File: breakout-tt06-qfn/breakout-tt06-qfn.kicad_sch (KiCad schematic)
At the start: 42 parts, among them J1 Conn_01x04, U1 Openframe_QFN_TT06_REV2, U2 24LC02

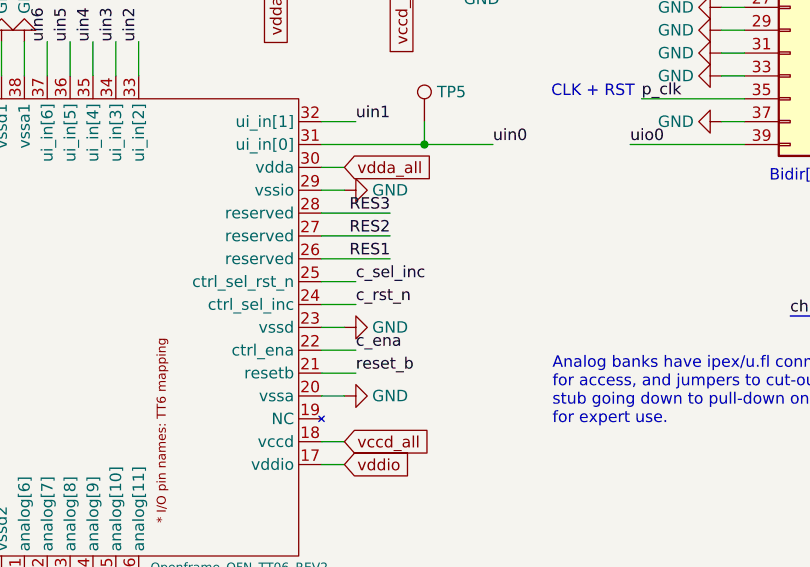
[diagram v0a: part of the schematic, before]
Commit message: CTRL MUX nReset and Increment lines crossed at chip: fixed
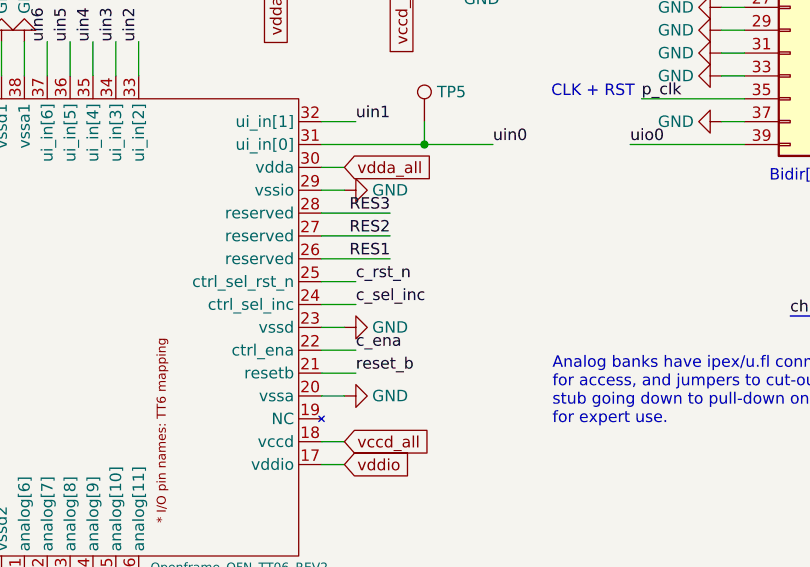
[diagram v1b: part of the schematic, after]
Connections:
- net c_rst_n: now also U1.25 (ctrl_sel_rst_n); no longer U1.24 (ctrl_sel_inc)
- net c_sel_inc: now also U1.24 (ctrl_sel_inc); no longer U1.25 (ctrl_sel_rst_n)
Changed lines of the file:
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@@
 	(title_block
 		(title "TT06 Openframe breakout")
-		(date "2024-08-10")
-		(rev "1.0")
+		(date "2024-11-04")
+		(rev "1.1")
 		(company "Psychogenic Technologies")
 		(comment 1 "(C) 2024 Pat Deegan")
@@
 		)
 	)
-	(label "c_sel_inc"
+	(label "c_rst_n"
 		(at 130.81 91.44 0)
 		(fields_autoplaced yes)
@@
 		)
 	)
-	(label "c_rst_n"
+	(label "c_sel_inc"
 		(at 130.81 93.98 0)
 		(fields_autoplaced yes)

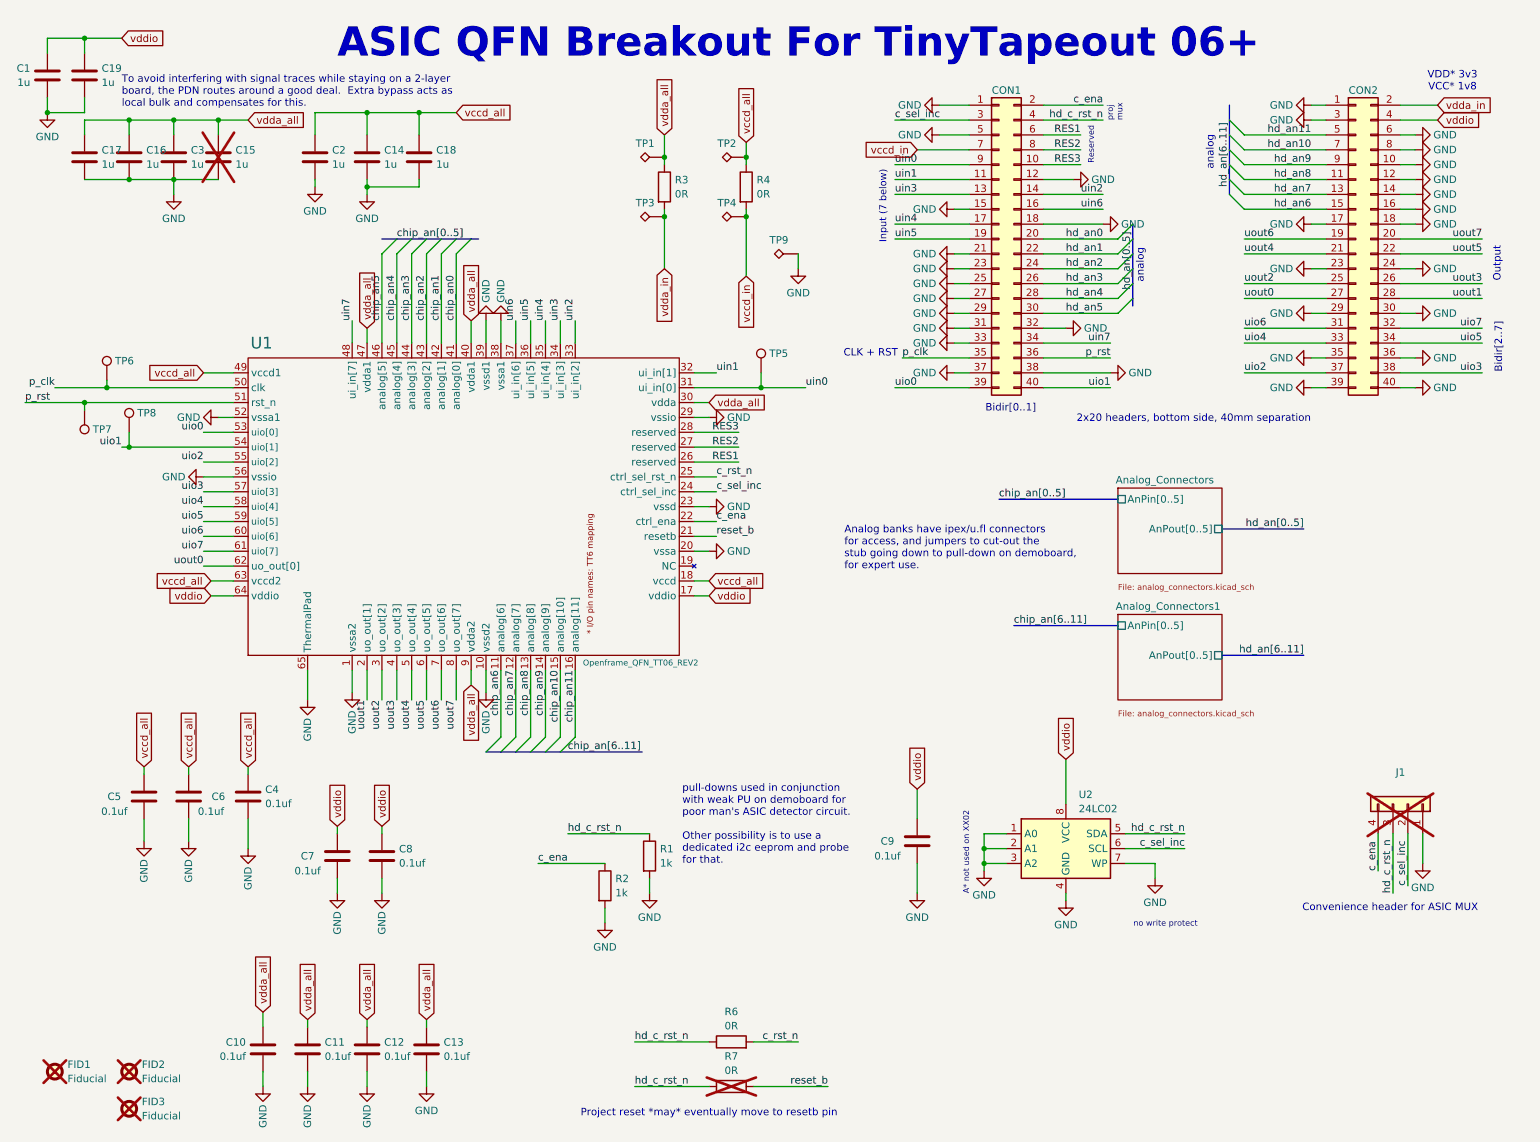
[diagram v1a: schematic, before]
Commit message: TT06 carrier v1.1 as in production run
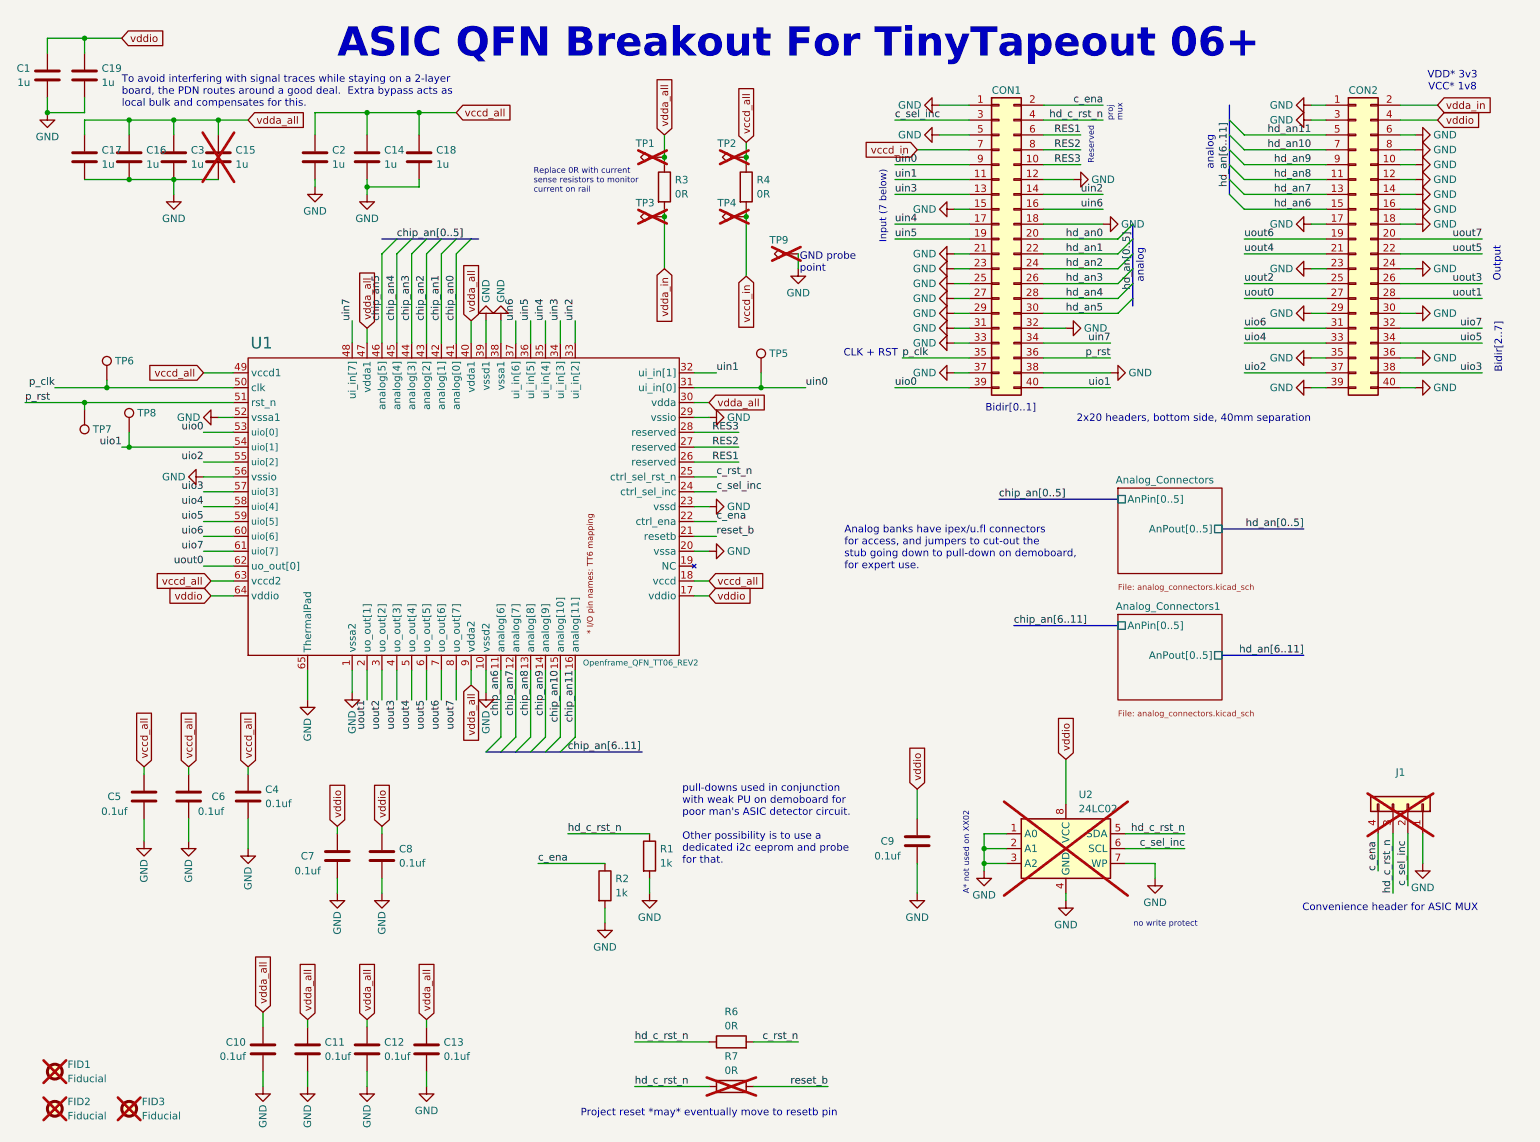
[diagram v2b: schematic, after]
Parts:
- C1, C14, C15, C16, C17, C18, C19, C2, C3: Characteristics (none) -> 1u 0603; LCSC (none) -> C5673
- C10, C11, C12, C13, C4, C5, C6, C7, C8, C9: Characteristics (none) -> 100n 0402; LCSC (none) -> C100072
- CON1: JLC C2685092 -> (none); LCSC (none) -> C2685092
- CON2: Characteristics (none) -> 2x20 100 mil Receptacle SMT; JLC C2685092 -> (none); LCSC (none) -> C2685092
- R1, R2: Characteristics (none) -> 1k 0402; LCSC (none) -> C202394
- R3, R4: Characteristics (none) -> 0R 1206
- R6, R7: Characteristics (none) -> 0R 0402
- TP1, TP2, TP3, TP4, TP9: LCSC (none) -> C238131; now not fitted
- U1: Characteristics (none) -> ASIC IC
- U2: Characteristics (none) -> I2C eeprom DFN 3x2; JLC C612280 -> (none); LCSC (none) -> C612280; now not fitted
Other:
- note added: "GND probe point"
- note added: "Replace 0R with current sense resistors to monitor current on rail"
- moved on the sheet: FID2
